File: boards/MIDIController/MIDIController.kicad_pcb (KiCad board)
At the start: 2 copper layers, 150 x 100 mm, 37 parts, among them J1 VBAT, J10 RJ45_Bel_SI-60062-F_fixed, J11 USB, J2 MIDICon, J3 IO_Boards, J4 USB_A, J5 I2S1, J6 I2S2, J7 Raspberry_Pi_2_3, J8 RPI_Pwr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

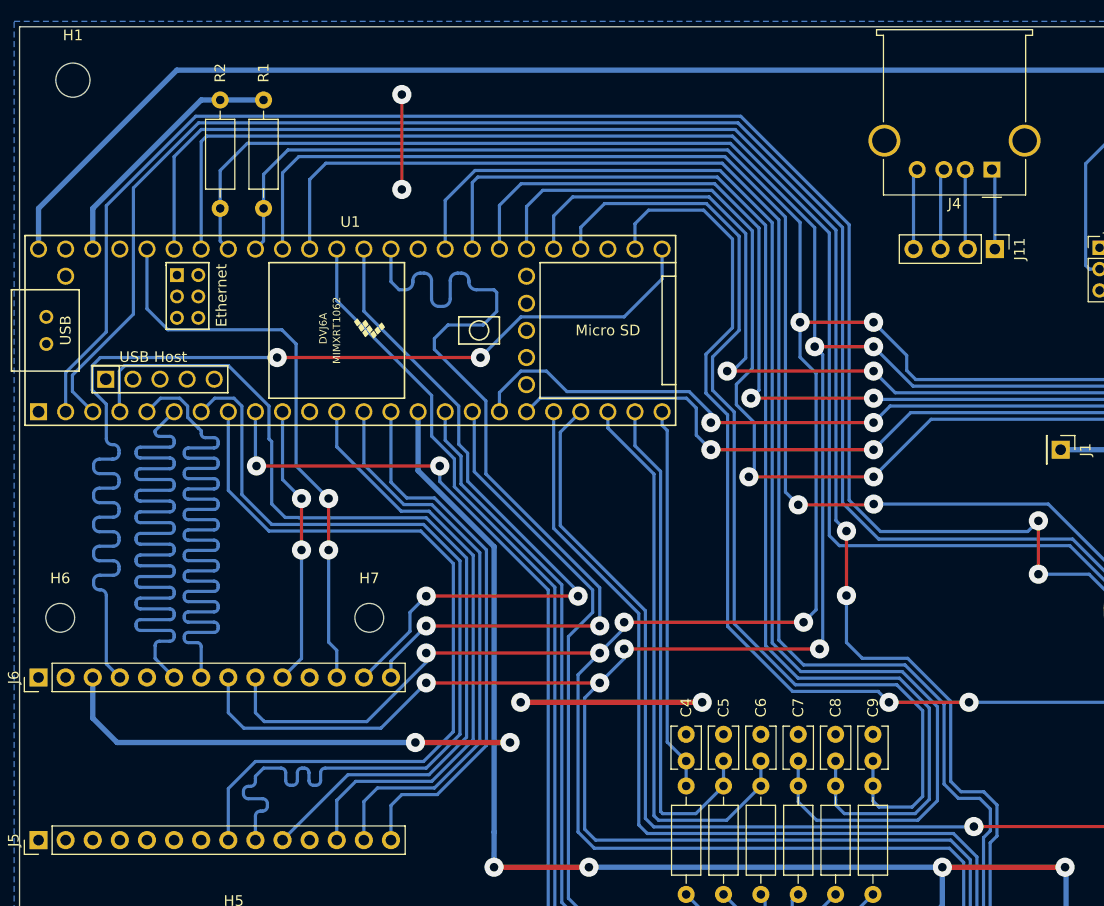
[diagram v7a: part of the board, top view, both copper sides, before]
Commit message: Fixed MIDIController I2S PCB, added LED
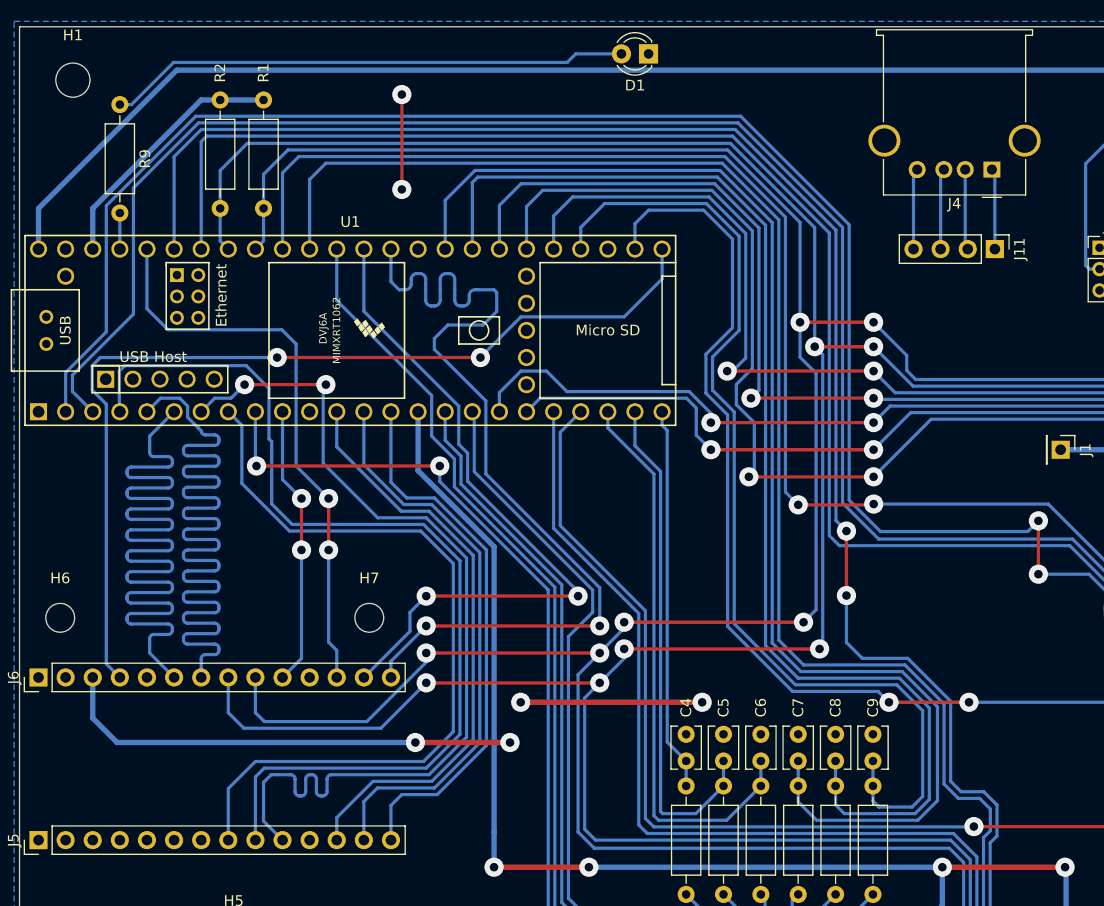
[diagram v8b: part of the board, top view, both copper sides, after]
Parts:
- added D1: LED, LED_THT:LED_D3.0mm, F.Cu at (125.5, 47.8)
- added R9: 4k7, Resistor_THT:R_Axial_DIN0207_L6.3mm_D2.5mm_P10.16mm_Horizontal, F.Cu at (75.9, 52.5)
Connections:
- J5 pad 10: /I2S_OUT2 -> /I2S_IN2
- J5 pad 9: /I2S_IN2 -> /I2S_OUT2
- U1 pad 45: unconnected-(U1-23_A9_CRX1_MCLK1-Pad45) -> /LED
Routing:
- net Net-(D1-A): track 0.00 -> 49.0 mm
- net /I2S_MCLK2: track 108.0 -> 89.8 mm
- net /I2S_OUT2: track 87.2 -> 93.4 mm
- net /I2S_BCLK2: track 86.6 -> 92.3 mm
- net /I2S_LRCLK2: track 86.6 -> 92.2 mm
- net /LED: track 0.00 -> 3.38 mm
- net /I2S_SCLK: track 84.6 -> 87.4 mm
- net /I2S_MEMCS: track 75.2 -> 74.0 mm
- net /I2S_CS: track 56.4 -> 55.5 mm
- net /I2S_IN2: track 86.9 -> 87.4 mm, vias 0 -> 2
